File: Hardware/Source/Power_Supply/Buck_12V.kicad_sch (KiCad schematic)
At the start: 0 parts

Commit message: Update Sche Power
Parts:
- added U2: TPS54331DR, charge_battery_footprint_lib:SOIC-8, symbol charge_battery_sym_lib:TPS54331DR
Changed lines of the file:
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@@
 	(generator_version "8.0")
 	(paper "A4")
+	(symbol
+		(lib_id "charge_battery_sym_lib:TPS54331DR")
+		(at 102.87 87.63 0)
+		(unit 1)
+		(exclude_from_sim no)
+		(in_bom yes)
+		(on_board yes)
+		(dnp no)
+		(fields_autoplaced yes)
+		(property "Reference" "U2"
+			(at 113.03 67.31 0)
+			(effects
+				(font
+					(size 1.27 1.27)
+				)
+			)
+		)
+		(property "Value" "TPS54331DR"
+			(at 113.03 69.85 0)
+			(effects
+				(font
+					(size 1.27 1.27)
+				)
+			)
+		)
+		(property "Footprint" "charge_battery_footprint_lib:SOIC-8"
+			(at 103.632 109.474 0)
+			(effects
+				(font
+					(size 1.27 1.27)
+				)
+				(hide yes)
+			)
+		)
+		(property "Datasheet" "http://www.ti.com/lit/ds/symlink/tps54336a.pdf"
+			(at 114.554 108.966 0)
+			(effects
+				(font
+					(size 1.27 1.27)
+				)
+				(hide yes)
+			)
+		)
+		(property "Description" "4.5V to 28V Input, 3A, Synchronous Step-Down Converter with Eco-mode(tm)"
+			(at 112.522 108.712 0)
+			(effects
+				(font
+					(size 1.27 1.27)
+				)
+				(hide yes)
+			)
+		)
+		(property "Supply name" "Thegioiic"
+			(at 91.694 109.728 0)
+			(effects
+				(font
+					(size 1.27 1.27)
+				)
+				(hide yes)
+			)
+		)
+		(property "Supply part name" "TPS54331DR IC Điều Chỉnh Giảm Áp 3A 8-SOIC"
+			(at 100.33 110.236 0)
+			(effects
+				(font
+					(size 1.27 1.27)
+				)
+				(hide yes)
+			)
+		)
+		(property "Supply URL" "https://thegioiic.com/tps54331dr-ic-dieu-chinh-giam-ap-3a-8-soic"
+			(at 107.442 109.982 0)
+			(effects
+				(font
+					(size 1.27 1.27)
+				)
+				(hide yes)
+			)
+		)
+		(pin "6"
+		)
+		(pin "3"
+		)
+		(pin "8"
+		)
+		(pin "4"
+		)
+		(pin "7"
+		)
+		(pin "2"
+		)
+		(pin "5"
+		)
+		(pin "1"
+		)
+		(instances
+			(project ""
+				(path "/5c8a7907-026b-4416-b231-5ef9f93b99e1/4f4f57c5-ff92-4f7f-a6cb-2a192931708c"
+					(reference "U2")
+					(unit 1)
+				)
+			)
+		)
+	)
 )

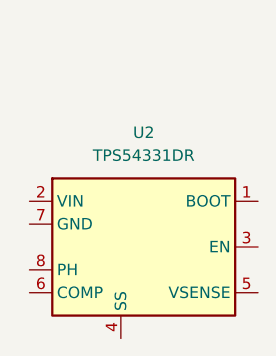
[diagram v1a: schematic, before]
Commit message: Update Sche 12V Power
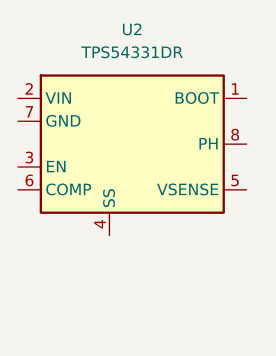
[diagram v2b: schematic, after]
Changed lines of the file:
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@@
 	(symbol
 		(lib_id "charge_battery_sym_lib:TPS54331DR")
-		(at 102.87 87.63 0)
+		(at 101.6 76.2 0)
 		(unit 1)
 		(exclude_from_sim no)
@@
 		(fields_autoplaced yes)
 		(property "Reference" "U2"
-			(at 113.03 67.31 0)
+			(at 111.76 55.88 0)
 			(effects
 				(font
@@
 		)
 		(property "Value" "TPS54331DR"
-			(at 113.03 69.85 0)
+			(at 111.76 58.42 0)
 			(effects
 				(font
@@
 		)
 		(property "Footprint" "charge_battery_footprint_lib:SOIC-8"
-			(at 103.632 109.474 0)
+			(at 102.362 98.044 0)
 			(effects
 				(font
@@
 		)
 		(property "Datasheet" "http://www.ti.com/lit/ds/symlink/tps54336a.pdf"
-			(at 114.554 108.966 0)
+			(at 113.284 97.536 0)
 			(effects
 				(font
@@
 		)
 		(property "Description" "4.5V to 28V Input, 3A, Synchronous Step-Down Converter with Eco-mode(tm)"
-			(at 112.522 108.712 0)
+			(at 111.252 97.282 0)
 			(effects
 				(font
@@
 		)
 		(property "Supply name" "Thegioiic"
-			(at 91.694 109.728 0)
+			(at 90.424 98.298 0)
 			(effects
 				(font
@@
 		)
 		(property "Supply part name" "TPS54331DR IC Điều Chỉnh Giảm Áp 3A 8-SOIC"
-			(at 100.33 110.236 0)
+			(at 99.06 98.806 0)
 			(effects
 				(font
@@
 		)
 		(property "Supply URL" "https://thegioiic.com/tps54331dr-ic-dieu-chinh-giam-ap-3a-8-soic"
-			(at 107.442 109.982 0)
+			(at 106.172 98.552 0)
 			(effects
 				(font
@@
 			)
 		)
-		(pin "6"
-		)
-		(pin "3"
+		(pin "1"
 		)
 		(pin "8"
 		)
+		(pin "5"
+		)
 		(pin "4"
+		)
+		(pin "6"
 		)
 		(pin "7"
@@
 		(pin "2"
 		)
-		(pin "5"
-		)
-		(pin "1"
+		(pin "3"
 		)
 		(instances

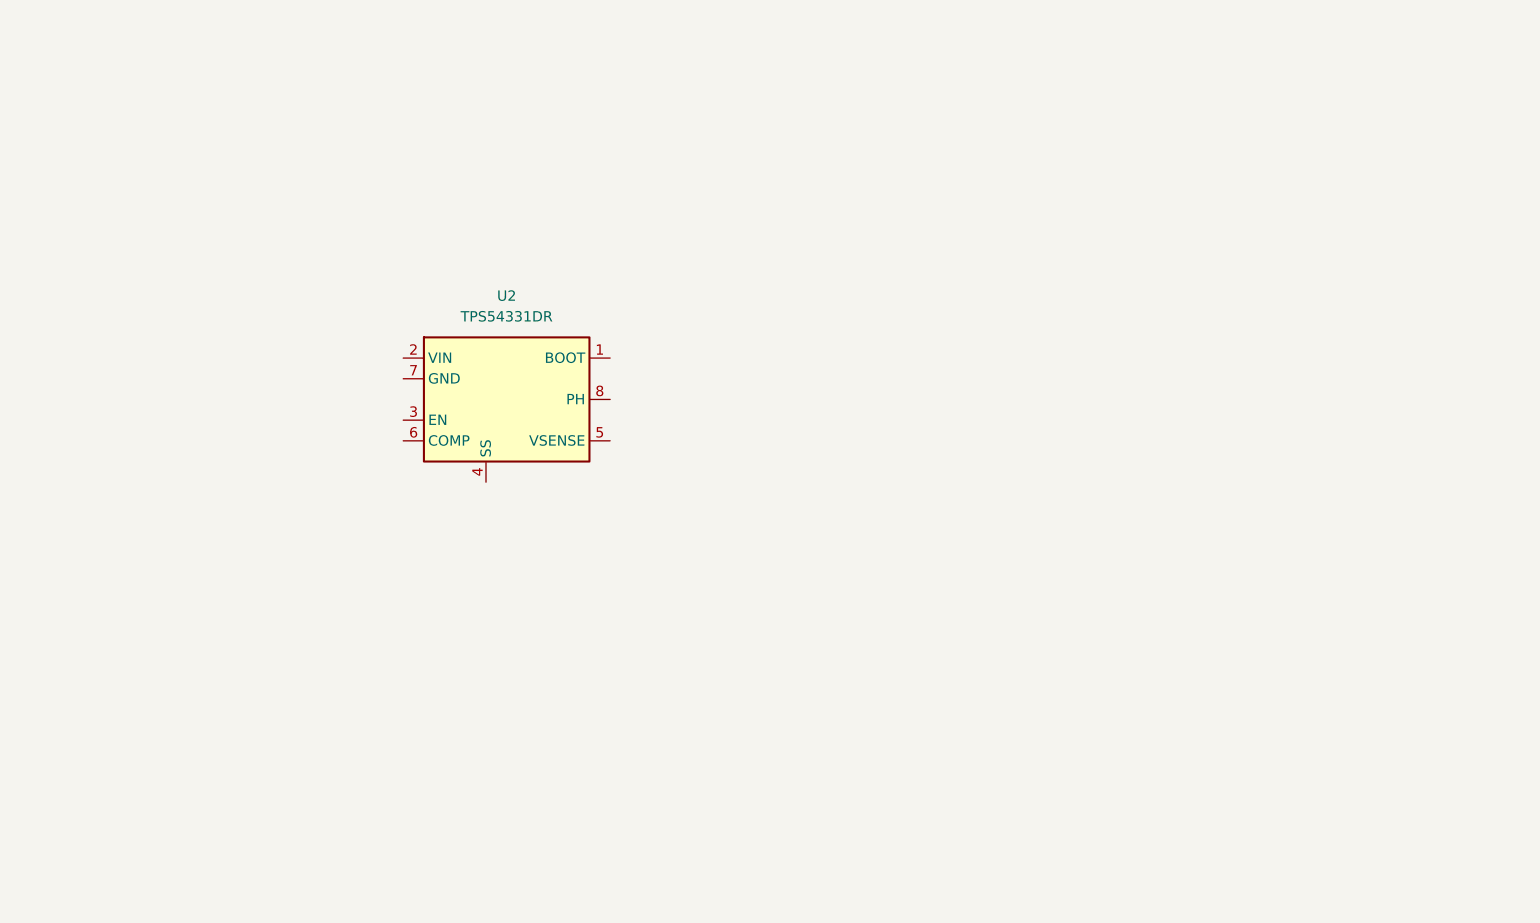
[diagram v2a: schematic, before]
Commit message: update sche buck 12v
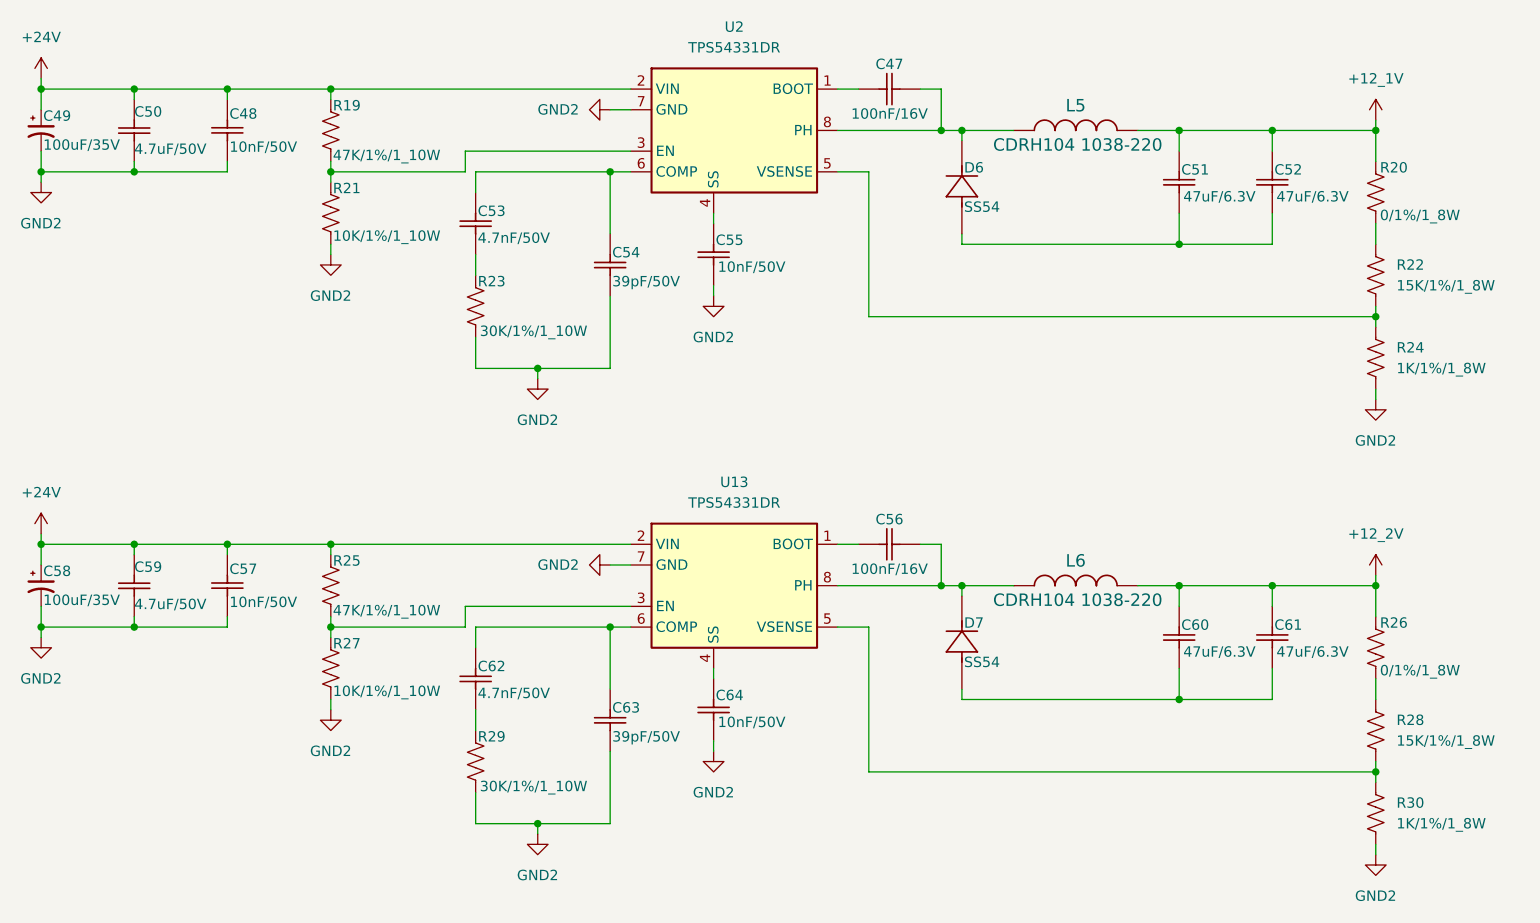
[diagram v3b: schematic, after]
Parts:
- added C47, C56: 100nF/16V, charge_battery_footprint_lib:Ceramic_Cap_0603, symbol charge_battery_sym_lib:Ceramic_Cap_SMD_100nF_16V
- added C48, C57: 10nF/50V, charge_battery_footprint_lib:Ceramic_Cap_0805, symbol charge_battery_sym_lib:Ceramic_Cap_SMD_10nF_50V_0805
- added C49, C58: 100uF/35V, Capacitor_SMD:CP_Elec_5x5.4, symbol charge_battery_sym_lib:Cap_Polarized_SMD_100uF_35V
- added C50, C59: 4.7uF/50V, charge_battery_footprint_lib:Ceramic_Cap_0805, symbol charge_battery_sym_lib:Ceramic_Cap_SMD_4.7uF_50V
- added C51, C52, C60, C61: 47uF/6.3V, charge_battery_footprint_lib:Ceramic_Cap_0805, symbol charge_battery_sym_lib:Ceramic_Cap_SMD_47uF_6.3V
- added C53, C62: 4.7nF/50V, charge_battery_footprint_lib:Ceramic_Cap_0603, symbol charge_battery_sym_lib:Ceramic_Cap_SMD_4.7nF_50V
- added C54, C63: 39pF/50V, charge_battery_footprint_lib:Ceramic_Cap_0603, symbol charge_battery_sym_lib:Ceramic_Cap_SMD_39pF_50V
- added C55, C64: 10nF/50V, charge_battery_footprint_lib:Ceramic_Cap_0603, symbol charge_battery_sym_lib:Ceramic_Cap_SMD_10nF_50V
- added D6, D7: SS54, charge_battery_footprint_lib:D_SMA, symbol charge_battery_sym_lib:SS54
- added L5, L6: CDRH104 1038-220, charge_battery_footprint_lib:CDRH104, symbol charge_battery_sym_lib:CDRH104 1038-220
- added R19, R25: 47K/1%/1_10W, charge_battery_footprint_lib:Res_0603, symbol charge_battery_sym_lib:Res_47K_0603_1%
- added R20, R26: 0/1%/1_8W, charge_battery_footprint_lib:Res_0805, symbol charge_battery_sym_lib:Res_0_0805_1%
- added R21, R27: 10K/1%/1_10W, charge_battery_footprint_lib:Res_0603, symbol charge_battery_sym_lib:Res_10K_0603_1%
- added R22, R28: 15K/1%/1_8W, charge_battery_footprint_lib:Res_0805, symbol charge_battery_sym_lib:Res_15K_0805_1%
- added R23, R29: 30K/1%/1_10W, charge_battery_footprint_lib:Res_0603, symbol charge_battery_sym_lib:Res_30K_0603_1%
- added R24, R30: 1K/1%/1_8W, charge_battery_footprint_lib:Res_0805, symbol charge_battery_sym_lib:Res_1K_0805_1%
- added U13: TPS54331DR, charge_battery_footprint_lib:SOIC-8, symbol charge_battery_sym_lib:TPS54331DR
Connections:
- net at U2.1 (BOOT): now also C47.1
- net +24V: now reaches U2.2 (VIN)
- net +24V: now also C48.1, C49.1, C50.2, C57.1, C58.1, C59.2, R19.2, R25.2, U13.2 (VIN)
- net at U2.3 (EN): now also R19.1, R21.2
- net at U2.4 (SS): now also C55.2
- net at U2.5 (VSENSE): now also R22.1, R24.2
- net at U2.6 (COMP): now also C53.2, C54.2
- net GND2: now reaches U2.7 (GND)
- net GND2: now also C48.2, C49.2, C50.1, C54.1, C55.1, C57.2, C58.2, C59.1, C63.1, C64.1, R21.1, R23.1, R24.1, R27.1, R29.1, R30.1, U13.7 (GND)
- net at U2.8 (PH): now also C47.2, D6.2 (K), L5.2
- new net: C62.2, C63.2, U13.6 (COMP)
- new net: C60.1, C61.1, D7.1 (A)
- new net: C56.2, D7.2 (K), L6.2, U13.8 (PH)
- new net: C51.1, C52.1, D6.1 (A)
- new net: C56.1, U13.1 (BOOT)
- new net: R28.1, R30.2, U13.5 (VSENSE)
- new net: R25.1, R27.2, U13.3 (EN)
- new net: C64.2, U13.4 (SS)
- new net: C53.1, R23.2
- new net: C62.1, R29.2
- new net: R20.1, R22.2
- new net: R26.1, R28.2
- new net +12_1V: C51.2, C52.2, L5.1, R20.2
- new net +12_2V: C60.2, C61.2, L6.1, R26.2
